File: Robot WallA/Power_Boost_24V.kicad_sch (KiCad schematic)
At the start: 33 parts, among them IC7 ABXS005A4X341-SRZ, Q2 BSS138, U2 125700D00000G, U3 125700D00000G

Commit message: Corrected all DRC erros, added info on PCB
modified distance meter connectors to be horizontal
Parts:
- HS1: footprint (none) -> Library:374524B60023G
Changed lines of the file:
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@@
 		(exclude_from_sim no)
 		(in_bom yes)
-		(on_board no)
+		(on_board yes)
 		(dnp no)
 		(fields_autoplaced yes)
@@
 			)
 		)
-		(property "Footprint" ""
+		(property "Footprint" "Library:374524B60023G"
 			(at 231.4448 134.62 0)
 			(effects

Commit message: Updated fab files.
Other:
- company: (none) -> Socotec Monitoring
- title: (none) -> Robot Wall-A

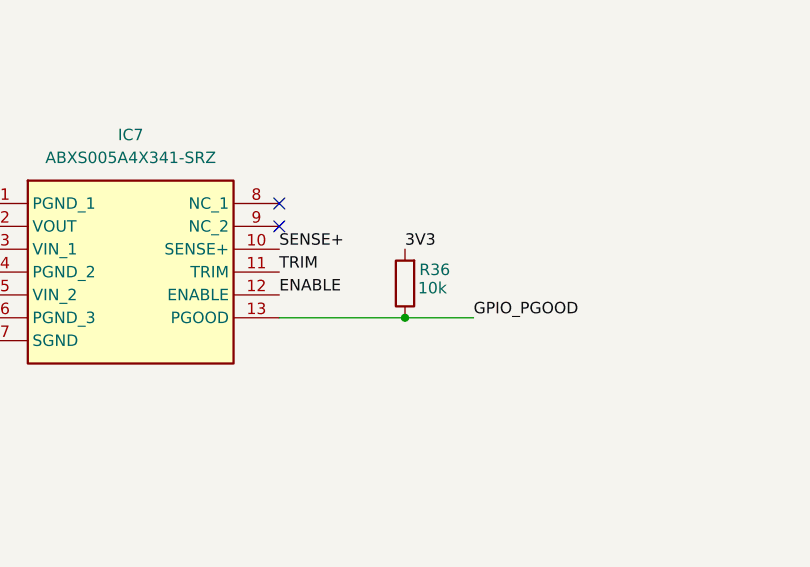
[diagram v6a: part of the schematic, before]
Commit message: Modified a bit pin header pins to allow I2C,SPI and CAN
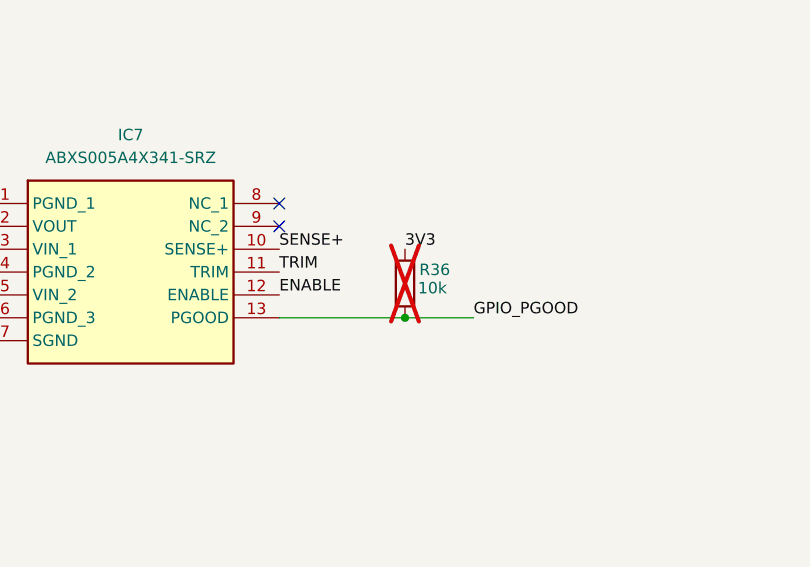
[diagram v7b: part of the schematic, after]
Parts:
- R36: now not fitted
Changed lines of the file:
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@@
 		(in_bom yes)
 		(on_board yes)
-		(dnp no)
+		(dnp yes)
 		(property "Reference" "R36"
 			(at 153.162 100.076 0)

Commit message: Modified footprint to simplify BOM. Finalized BOM.
Updated fab files
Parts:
- C63, C64, C65, C66, C67: Manufacturer_Part_Number (none) -> GRM21BR61H475ME51L
- C68: Manufacturer_Part_Number (none) -> CL21B103KBANNNC
- C70, C71, C72, C73, C74, C75, C76: value 47nF/25V -> 47nF/50V; Manufacturer_Part_Number (none) -> CC0603KPX7R9BB473
- C77, C78, C79, C80, C81: value 4.7uF/25V -> 4.7uF/50V; Manufacturer_Part_Number (none) -> GRM32ER71H475KA88L
- C82: Manufacturer_Part_Number (none) -> C0603C471K5RACTU
- R33: value 11.1k -> 11.3k; Manufacturer_Part_Number (none) -> CRCW060311K3FKEA
- R34: Manufacturer_Part_Number (none) -> CRCW0603200KFKEC
- R35: Manufacturer_Part_Number (none) -> RCA0603100KFKEAHP
- R36, R38: Manufacturer_Part_Number (none) -> 667-ERJ-3GEYJ103V
- R37: value 10,553k/1% -> 10,553k/0.5%; Manufacturer_Part_Number (none) -> RC0603DR-0710K5L
